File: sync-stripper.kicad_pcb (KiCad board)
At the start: 2 copper layers, 32 x 19 mm, 11 parts, among them J1 5V, J2 SYNC, J3 VIDEO, J4 GND, U1 LM1881

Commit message: Use ground/vcc symbols rather than labels
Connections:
- net 5Vin renamed +5V
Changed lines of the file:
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@@
 	(net 2 "VIDEO")
 	(net 3 "GND")
-	(net 4 "5Vin")
+	(net 4 "+5V")
 	(net 5 "Net-(U1-BURST)")
 	(net 6 "Net-(U1-CSYNC)")
@@
 			(layers "F.Cu" "F.Mask" "F.Paste")
 			(roundrect_rratio 0.25)
-			(net 4 "5Vin")
+			(net 4 "+5V")
 			(pintype "passive")
 		)
@@
 			(layers "F.Cu" "F.Mask" "F.Paste")
 			(roundrect_rratio 0.25)
-			(net 4 "5Vin")
+			(net 4 "+5V")
 			(pinfunction "Pin_1")
 			(pintype "passive")
@@
 			(layers "F.Cu" "F.Mask" "F.Paste")
 			(roundrect_rratio 0.25)
-			(net 4 "5Vin")
+			(net 4 "+5V")
 			(pinfunction "VCC")
 			(pintype "power_in")

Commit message: More compact design
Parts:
- moved 5V 24.0 mm to (127.0, 88.7), turned to 90 degrees
- moved GND 23.0 mm to (127.0, 97.0)
- moved R2 13.9 mm to (117.1, 97.0)
- moved OUT 10.4 mm to (107.0, 97.0)
- moved R1 6.28 mm to (110.9, 88.0), turned to 0 degrees
- moved IN 5.00 mm to (107.0, 88.0)
- moved R3 1.90 mm to (126.1, 93.4)
- moved C1 0.86 mm to (110.9, 90.0)
- renumbered J1 to 5V, J4 to GND, J3 to IN, J2 to OUT
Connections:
- net SYNC renamed Net-(J2-Pin_1)
- net VIDEO renamed Net-(J3-Pin_1)
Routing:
- net +5V: track 23.4 -> 7.23 mm
- net Net-(U1-CSYNC): track 6.29 -> 10.2 mm
- net Net-(J3-Pin_1): track 8.71 -> 5.00 mm
- net Net-(J2-Pin_1): track 5.92 -> 9.17 mm
- net Net-(U1-BURST): track 8.19 -> 6.29 mm
- net Net-(U1-VIDEO): track 3.96 -> 3.10 mm
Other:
- board size 32 x 19 mm -> 26 x 14 mm

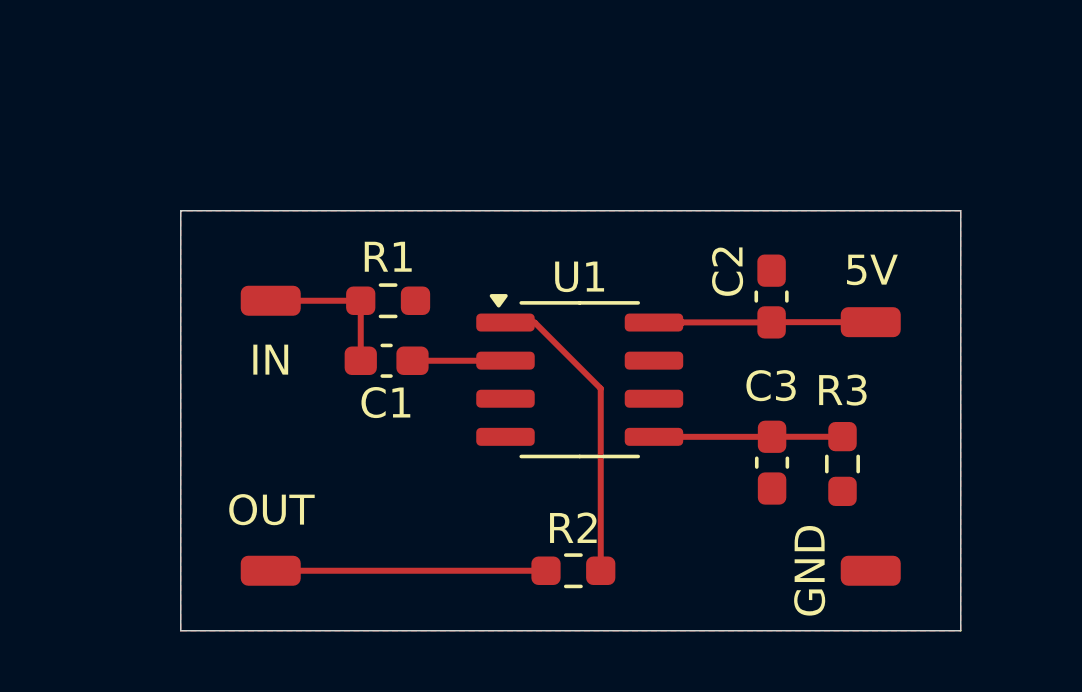
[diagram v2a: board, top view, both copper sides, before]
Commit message: As compact as I can get it
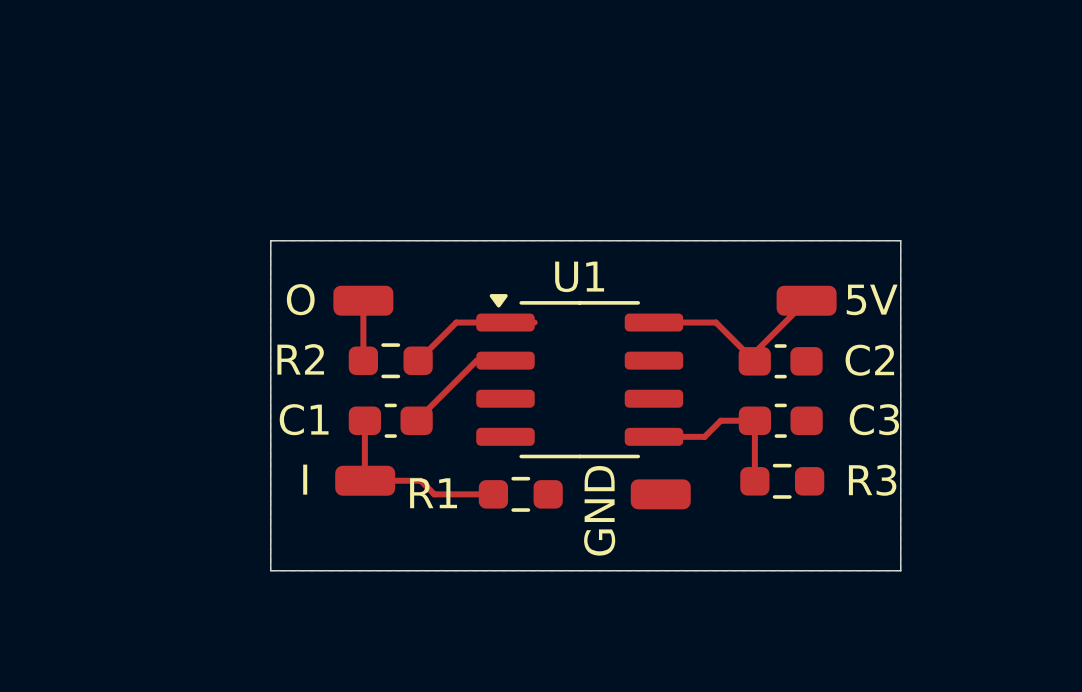
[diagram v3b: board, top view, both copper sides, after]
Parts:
- moved O 9.52 mm to (110.1, 88.0)
- moved R2 9.28 mm to (111.0, 90.0)
- moved R1 7.82 mm to (115.3, 94.5)
- moved GND 7.45 mm to (120.0, 94.5), turned to 90 degrees
- moved I 6.78 mm to (110.1, 94.0)
- moved 5V 2.25 mm to (124.9, 88.0)
- moved C2 2.18 mm to (124.0, 90.0), turned to 0 degrees
- moved R3 2.09 mm to (124.0, 94.0), turned to 0 degrees
- moved C1 2.00 mm to (111.0, 92.0)
- moved C3 1.43 mm to (124.0, 92.0), turned to 0 degrees
- renumbered IN to I, OUT to O
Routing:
- net Net-(J2-Pin_1): track 9.17 -> 2.00 mm
- net Net-(U1-CSYNC): track 10.2 -> 4.41 mm
- net Net-(J3-Pin_1): track 5.00 -> 6.48 mm
- net Net-(U1-VIDEO): track 3.10 -> 3.80 mm
- net Net-(U1-BURST): track 6.29 -> 5.60 mm
- net +5V: track 7.23 -> 6.63 mm
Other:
- board size 26 x 14 mm -> 21 x 11 mm

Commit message: No but really, super tiny
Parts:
- renumbered GND to G
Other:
- board size 21 x 11 mm -> 21 x 10 mm
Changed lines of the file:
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@@
 		(descr "Wire Pad, Square, SMD Pad,  1mm x 2mm,")
 		(tags "MesurementPoint Square SMDPad 1mmx2mm ")
-		(property "Reference" "GND"
+		(property "Reference" "G"
 			(at -0.546302 -2 90)
 			(layer "F.SilkS")
@@
 	(gr_rect
 		(start 107 86)
-		(end 128 97)
+		(end 128 96)
 		(stroke
 			(width 0.05)
@@
 		(polygon
 			(pts
-				(xy 107 86) (xy 107 97) (xy 128 97) (xy 128 86)
-			)
-		)
+				(xy 107 86) (xy 107 96) (xy 128 96) (xy 128 86)
+			)
+		)

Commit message: More sensible layout
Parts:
- moved G 4.89 mm to (124.9, 94.0), turned to -90 degrees
- moved R3 4.72 mm to (119.4, 94.5), turned to 180 degrees
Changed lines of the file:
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@@
 	(footprint "Resistor_SMD:R_0603_1608Metric_Pad0.98x0.95mm_HandSolder"
 		(layer "F.Cu")
-		(at 124.049576 94.019025)
+		(at 119.353431 94.452968 180)
 		(descr "Resistor SMD 0603 (1608 Metric), square (rectangular) end terminal, IPC_7351 nominal with elongated pad for handsoldering. (Body size source: IPC-SM-782 page 72, https://www.pcb-3d.com/wordpress/wp-content/uploads/ipc-sm-782a_amendment_1_and_2.pdf), generated with kicad-footprint-generator")
 		(tags "resistor handsolder")
 		(property "Reference" "R3"
-			(at 3 0 180)
+			(at -2.646569 0 0)
 			(layer "F.SilkS")
 			(effects
@@
 		)
 		(property "Datasheet" ""
-			(at 0 0 0)
+			(at 0 0 180)
 			(unlocked yes)
 			(layer "F.Fab")
@@
 		)
 		(property "Description" "Resistor, US symbol"
-			(at 0 0 0)
+			(at 0 0 180)
 			(unlocked yes)
 			(layer "F.Fab")
@@
 		(attr smd)
 		(fp_line
+			(start -0.254724 0.5225)
+			(end 0.254724 0.5225)
+			(stroke
+				(width 0.12)
+				(type solid)
+			)
+			(layer "F.SilkS")
+		)
+		(fp_line
 			(start -0.254724 -0.5225)
 			(end 0.254724 -0.5225)
@@
 		)
 		(fp_line
-			(start -0.254724 0.5225)
-			(end 0.254724 0.5225)
-			(stroke
-				(width 0.12)
-				(type solid)
-			)
-			(layer "F.SilkS")
+			(start 1.65 0.73)
+			(end -1.65 0.73)
+			(stroke
+				(width 0.05)
+				(type solid)
+			)
+			(layer "F.CrtYd")
+		)
+		(fp_line
+			(start 1.65 -0.73)
+			(end 1.65 0.73)
+			(stroke
+				(width 0.05)
+				(type solid)
+			)
+			(layer "F.CrtYd")
+		)
+		(fp_line
+			(start -1.65 0.73)
+			(end -1.65 -0.73)
+			(stroke
+				(width 0.05)
+				(type solid)
+			)
+			(layer "F.CrtYd")
 		)
 		(fp_line
@@
 		)
 		(fp_line
-			(start -1.65 0.73)
-			(end -1.65 -0.73)
-			(stroke
-				(width 0.05)
-				(type solid)
-			)
-			(layer "F.CrtYd")
-		)
-		(fp_line
-			(start 1.65 -0.73)
-			(end 1.65 0.73)
-			(stroke
-				(width 0.05)
-				(type solid)
-			)
-			(layer "F.CrtYd")
-		)
-		(fp_line
-			(start 1.65 0.73)
-			(end -1.65 0.73)
-			(stroke
-				(width 0.05)
-				(type solid)
-			)
-			(layer "F.CrtYd")
+			(start 0.8 0.4125)
+			(end -0.8 0.4125)
+			(stroke
+				(width 0.1)
+				(type solid)
+			)
+			(layer "F.Fab")
+		)
+		(fp_line
+			(start 0.8 -0.4125)
+			(end 0.8 0.4125)
+			(stroke
+				(width 0.1)
+				(type solid)
+			)
+			(layer "F.Fab")
+		)
+		(fp_line
+			(start -0.8 0.4125)
+			(end -0.8 -0.4125)
+			(stroke
+				(width 0.1)
+				(type solid)
+			)
+			(layer "F.Fab")
 		)
 		(fp_line
@@
 			(layer "F.Fab")
 		)
-		(fp_line
-			(start -0.8 0.4125)
-			(end -0.8 -0.4125)
-			(stroke
-				(width 0.1)
-				(type solid)
-			)
-			(layer "F.Fab")
-		)
-		(fp_line
-			(start 0.8 -0.4125)
-			(end 0.8 0.4125)
-			(stroke
-				(width 0.1)
-				(type solid)
-			)
-			(layer "F.Fab")
-		)
-		(fp_line
-			(start 0.8 0.4125)
-			(end -0.8 0.4125)
-			(stroke
-				(width 0.1)
-				(type solid)
-			)
-			(layer "F.Fab")
-		)
 		(fp_text user "${REFERENCE}"
 			(at 0 0 0)
@@
 		)
 		(pad "1" smd roundrect
-			(at -0.9125 0)
+			(at -0.9125 0 180)
 			(size 0.975 0.95)
 			(layers "F.Cu" "F.Mask" "F.Paste")
@@
 		)
 		(pad "2" smd roundrect
-			(at 0.9125 0)
+			(at 0.9125 0 180)
 			(size 0.975 0.95)
 			(layers "F.Cu" "F.Mask" "F.Paste")
@@
 	(footprint "Connector_Wire:SolderWirePad_1x01_SMD_1x2mm"
 		(layer "F.Cu")
-		(at 120 94.453698 90)
+		(at 124.87141 93.979031 -90)
 		(descr "Wire Pad, Square, SMD Pad,  1mm x 2mm,")
 		(tags "MesurementPoint Square SMDPad 1mmx2mm ")
 		(property "Reference" "G"
-			(at -0.546302 -2 90)
+			(at -0.016196 -1.983748 0)
 			(layer "F.SilkS")
 			(effects
@@
 		)
 		(property "Datasheet" ""
-			(at 0 0 90)
+			(at 0 0 270)
 			(unlocked yes)
 			(layer "F.Fab")
@@
 		)
 		(property "Description" "Generic connector, single row, 01x01, script generated"
-			(at 0 0 90)
+			(at 0 0 270)
 			(unlocked yes)
 			(layer "F.Fab")
@@
 		(attr exclude_from_pos_files)
 		(fp_line
+			(start -0.63 1.27)
+			(end 0.63 1.27)
+			(stroke
+				(width 0.05)
+				(type solid)
+			)
+			(layer "F.CrtYd")
+		)
+		(fp_line
+			(start 0.63 1.27)
+			(end 0.63 -1.27)
+			(stroke
+				(width 0.05)
+				(type solid)
+			)
+			(layer "F.CrtYd")
+		)
+		(fp_line
+			(start -0.63 -1.27)
+			(end -0.63 1.27)
+			(stroke
+				(width 0.05)
+				(type solid)
+			)
+			(layer "F.CrtYd")
+		)
+		(fp_line
 			(start 0.63 -1.27)
 			(end -0.63 -1.27)
@@
 		)
 		(fp_line
+			(start -0.63 1.27)
+			(end -0.63 -1.27)
+			(stroke
+				(width 0.1)
+				(type solid)
+			)
+			(layer "F.Fab")
+		)
+		(fp_line
+			(start 0.63 1.27)
+			(end -0.63 1.27)
+			(stroke
+				(width 0.1)
+				(type solid)
+			)
+			(layer "F.Fab")
+		)
+		(fp_line
 			(start -0.63 -1.27)
-			(end -0.63 1.27)
-			(stroke
-				(width 0.05)
-				(type solid)
-			)
-			(layer "F.CrtYd")
-		)
-		(fp_line
-			(start 0.63 1.27)
 			(end 0.63 -1.27)
 			(stroke
-				(width 0.05)
-				(type solid)
-			)
-			(layer "F.CrtYd")
-		)
-		(fp_line
-			(start -0.63 1.27)
-			(end 0.63 1.27)
-			(stroke
-				(width 0.05)
-				(type solid)
-			)
-			(layer "F.CrtYd")
+				(width 0.1)
+				(type solid)
+			)
+			(layer "F.Fab")
 		)
 		(fp_line
@@
 			(layer "F.Fab")
 		)
-		(fp_line
-			(start -0.63 -1.27)
-			(end 0.63 -1.27)
-			(stroke
-				(width 0.1)
-				(type solid)
-			)
-			(layer "F.Fab")
-		)
-		(fp_line
-			(start 0.63 1.27)
-			(end -0.63 1.27)
-			(stroke
-				(width 0.1)
-				(type solid)
-			)
-			(layer "F.Fab")
-		)
-		(fp_line
-			(start -0.63 1.27)
-			(end -0.63 -1.27)
-			(stroke
-				(width 0.1)
-				(type solid)
-			)
-			(layer "F.Fab")
-		)
 		(pad "1" smd roundrect
-			(at 0 0 90)
+			(at 0 0 270)
 			(size 1 2)
 			(layers "F.Cu" "F.Mask" "F.Paste")
@@
 	)
 	(segment
-		(start 123.1375 94.018601)
-		(end 123.137076 94.019025)
+		(start 120.265931 93.028167)
+		(end 120.265931 94.452968)
 		(width 0.2)
 		(layer "F.Cu")
@@
 	)
 	(segment
-		(start 123.1375 92)
-		(end 123.1375 94.018601)
-		(width 0.2)
-		(layer "F.Cu")
+		(start 119.774169 92.536405)
+		(end 120.265931 93.028167)
+		(width 0.2)
+		(layer "F.Cu")

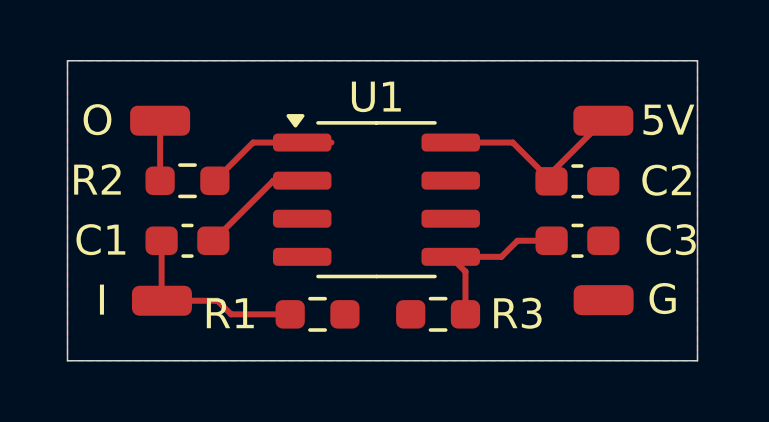
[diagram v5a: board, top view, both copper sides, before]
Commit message: Remove KiCad BOM, remove Rset usage, add second ground plane and ground vias
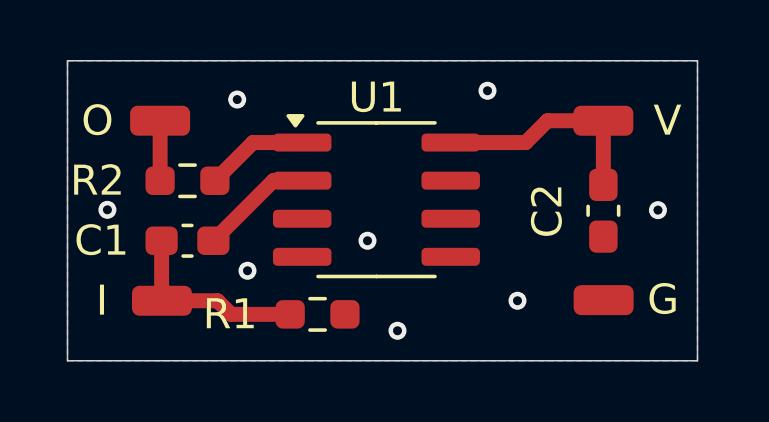
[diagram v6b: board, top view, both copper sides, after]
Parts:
- removed C3: 100n, Capacitor_SMD:C_0603_1608Metric_Pad1.08x0.95mm_HandSolder
- removed R3: 680k, Resistor_SMD:R_0603_1608Metric_Pad0.98x0.95mm_HandSolder
- moved C2 1.31 mm to (124.9, 91.0), turned to -90 degrees
- renumbered 5V to V
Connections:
- U1 pad 5: Net-(U1-BURST) -> unconnected-(U1-BPOUT-Pad5)
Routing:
- net Net-(U1-BURST): track 5.71 -> 0.00 mm
- net Net-(U1-CSOUT): track 4.41 -> 3.44 mm
- net +5V: track 6.63 -> 7.53 mm
- net GND: vias 0 -> 8
- added copper zone on B.Cu, net GND
